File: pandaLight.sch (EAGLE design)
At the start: 162 parts, among them J1 PJ-037A, X1 USBUB-S, X2 HDMI_RECEPTICAL_A, X3 HDMI_RECEPTICAL_A, X4 HDMI_RECEPTICAL_A, Y1 403, Y2 20Mhz

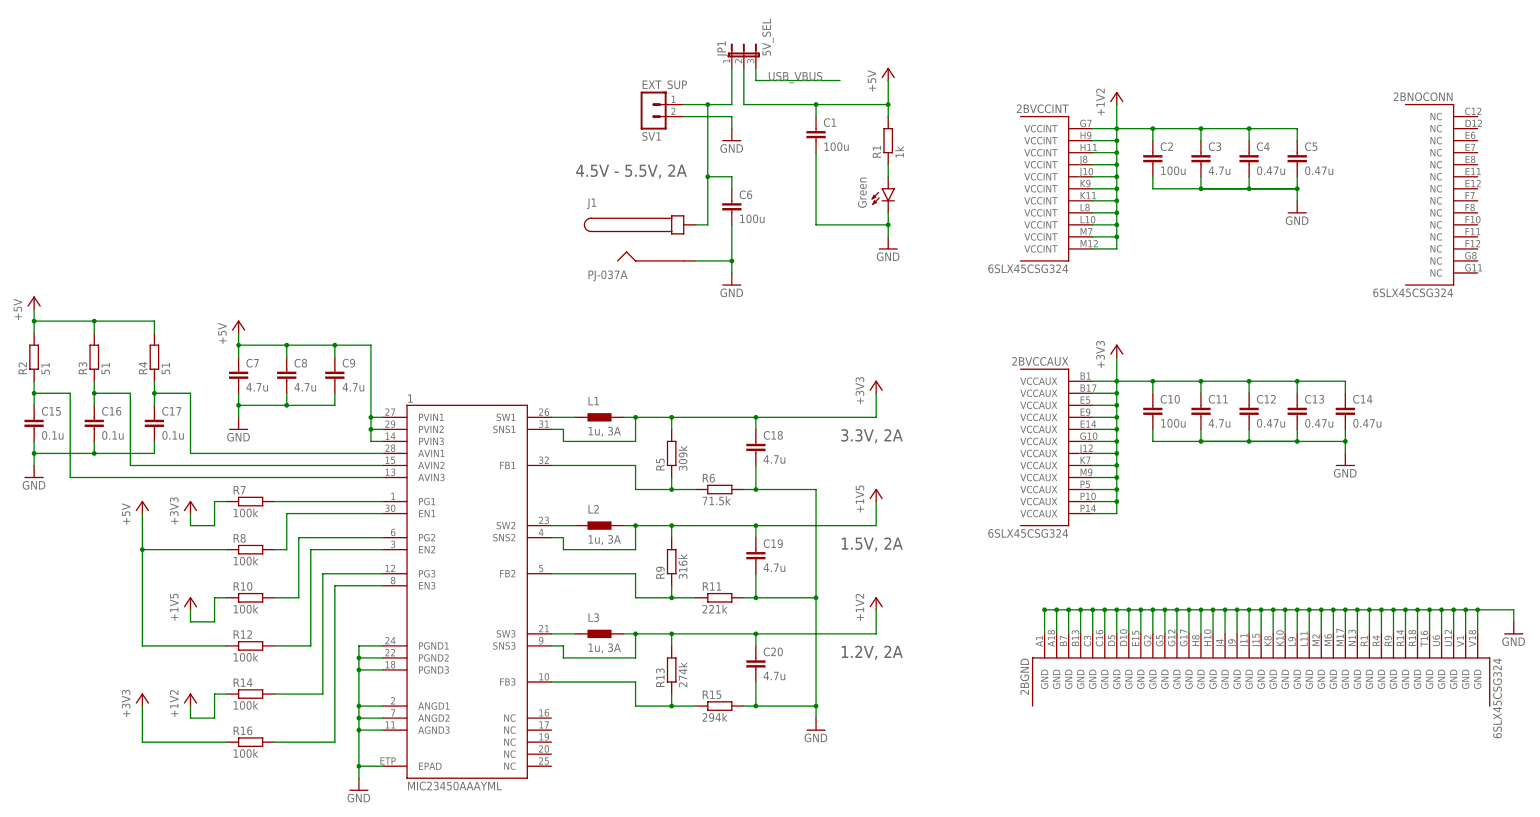
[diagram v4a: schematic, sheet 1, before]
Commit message: Routed the new buck regulator
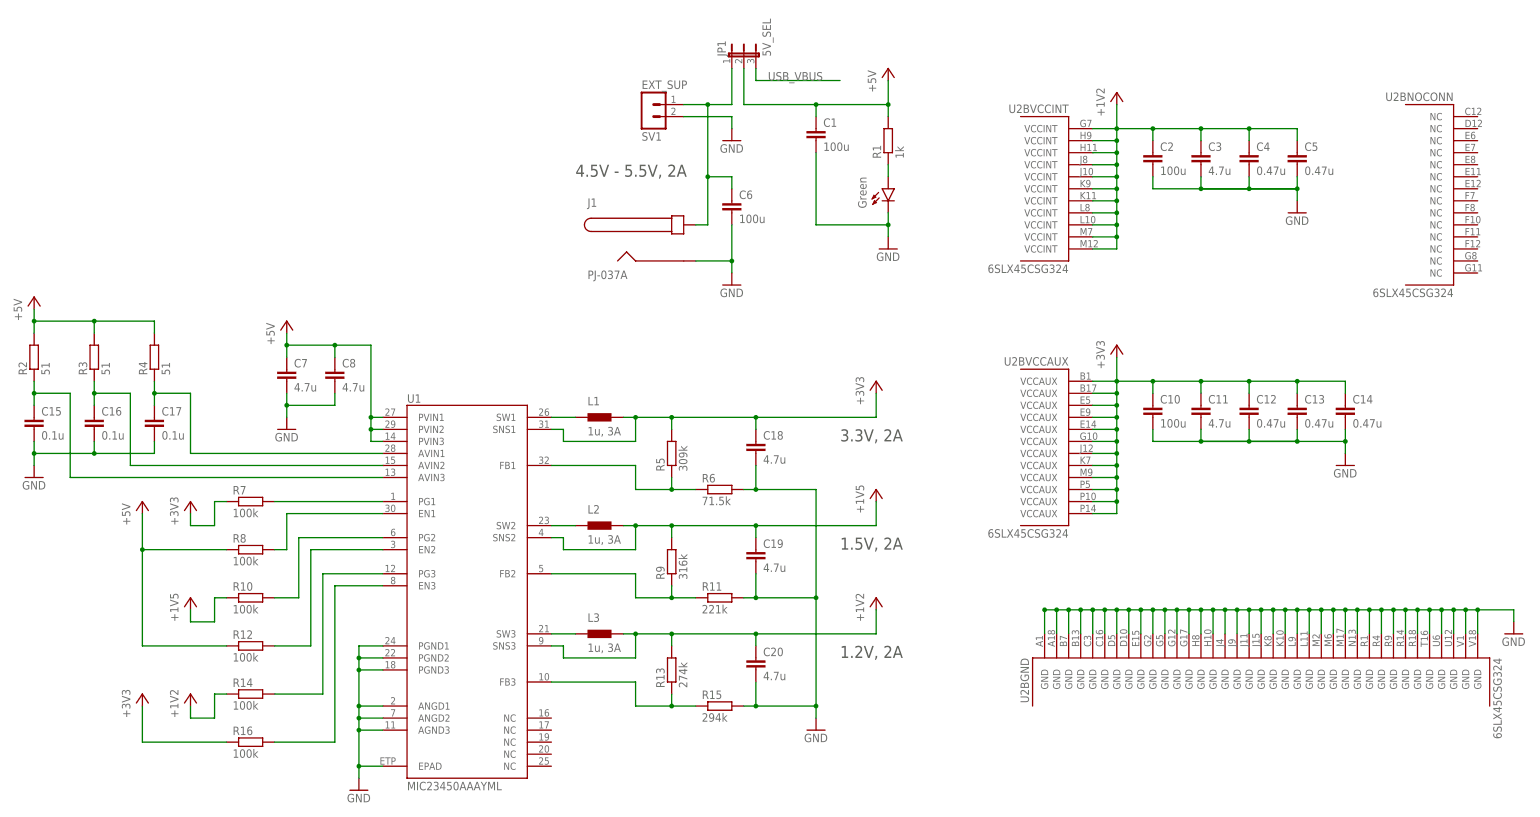
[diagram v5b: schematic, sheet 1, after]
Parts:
- removed C9: 4.7u, pandaLight:CAPACITOR0603
- renumbered 1 to U1, 10 to U10, 11 to U11, 12 to U12, 13 to U13, 14 to U14, 15 to U15, 16 to U16, 17 to U17, 18 to U18, 2 to U2, 3 to U3, 4 to U4, 5 to U5, 6 to U6, 7 to U7, 8 to U8, 9 to U9
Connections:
- net +5V: no longer C9.1
- net GND: no longer C9.2
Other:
- moved on the sheet: C7, C8

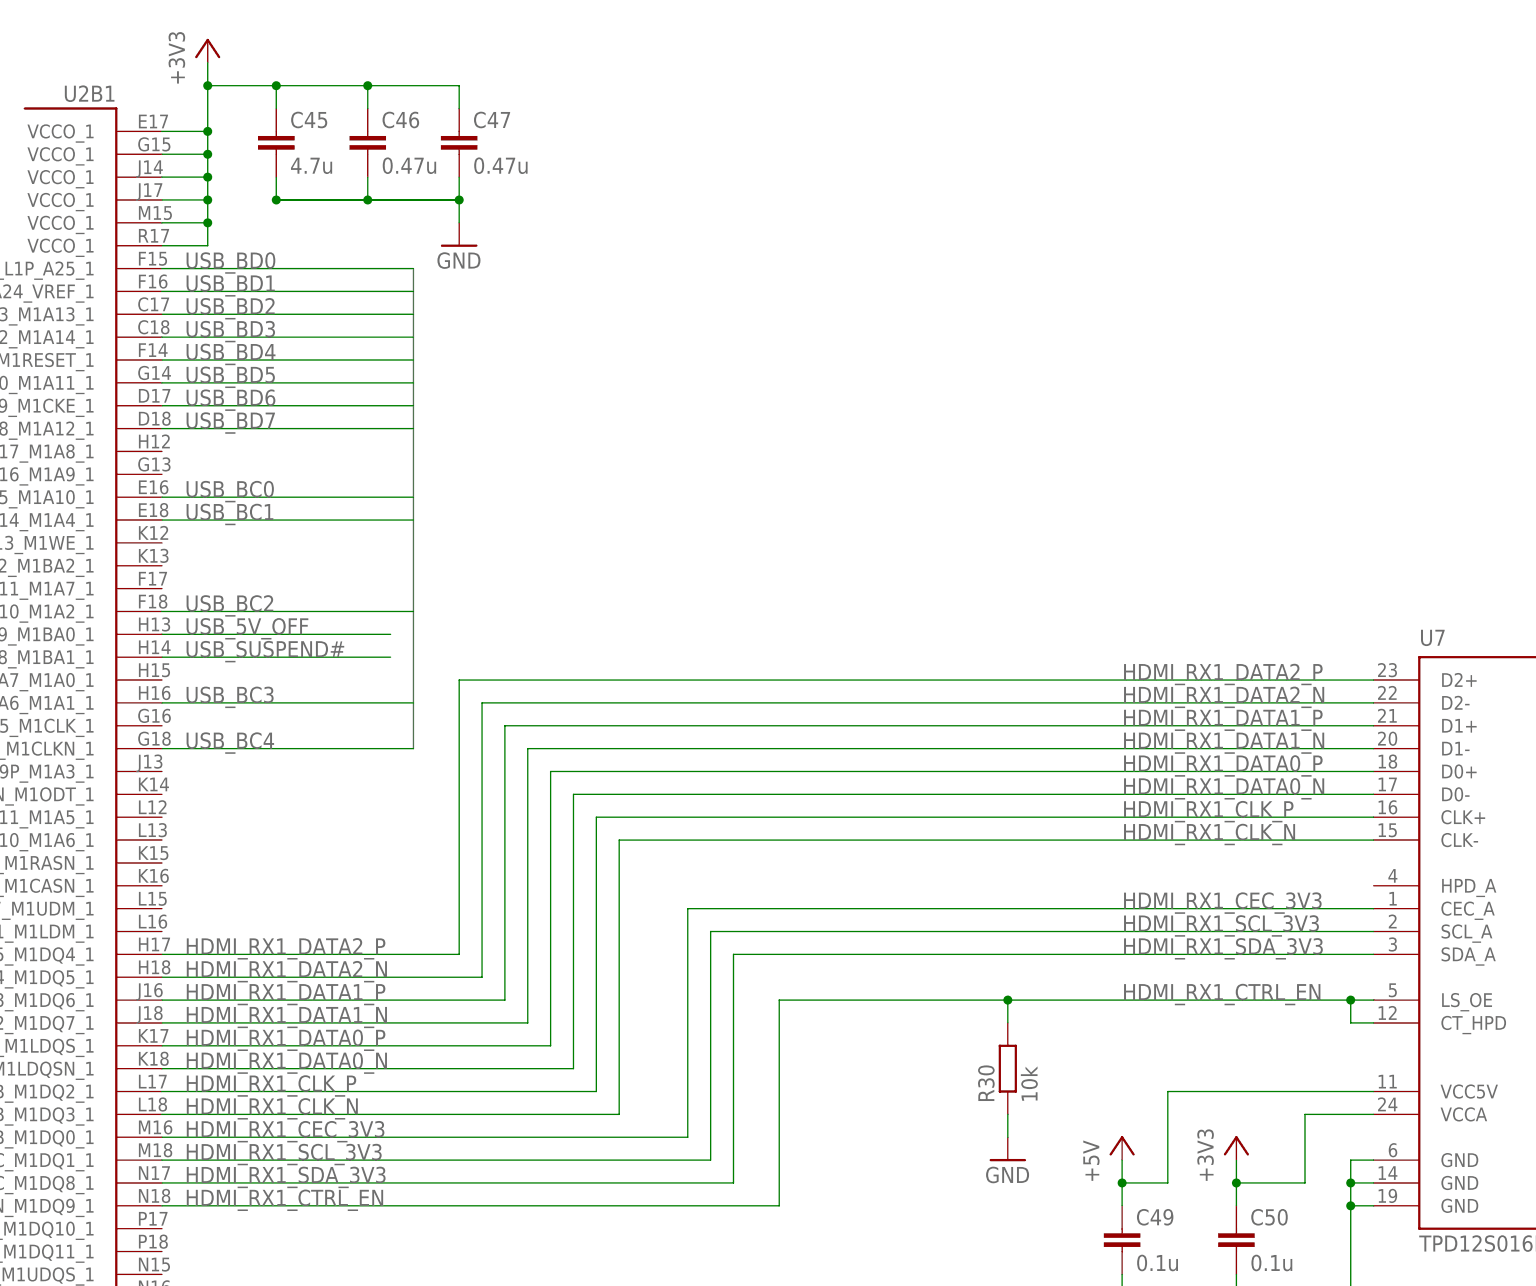
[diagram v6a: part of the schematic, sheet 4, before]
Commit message: Temporarily unconnected the PMOD and USB to FPGA wires; Moved power management and USB a little closer together; Began routing HDMI_RX1
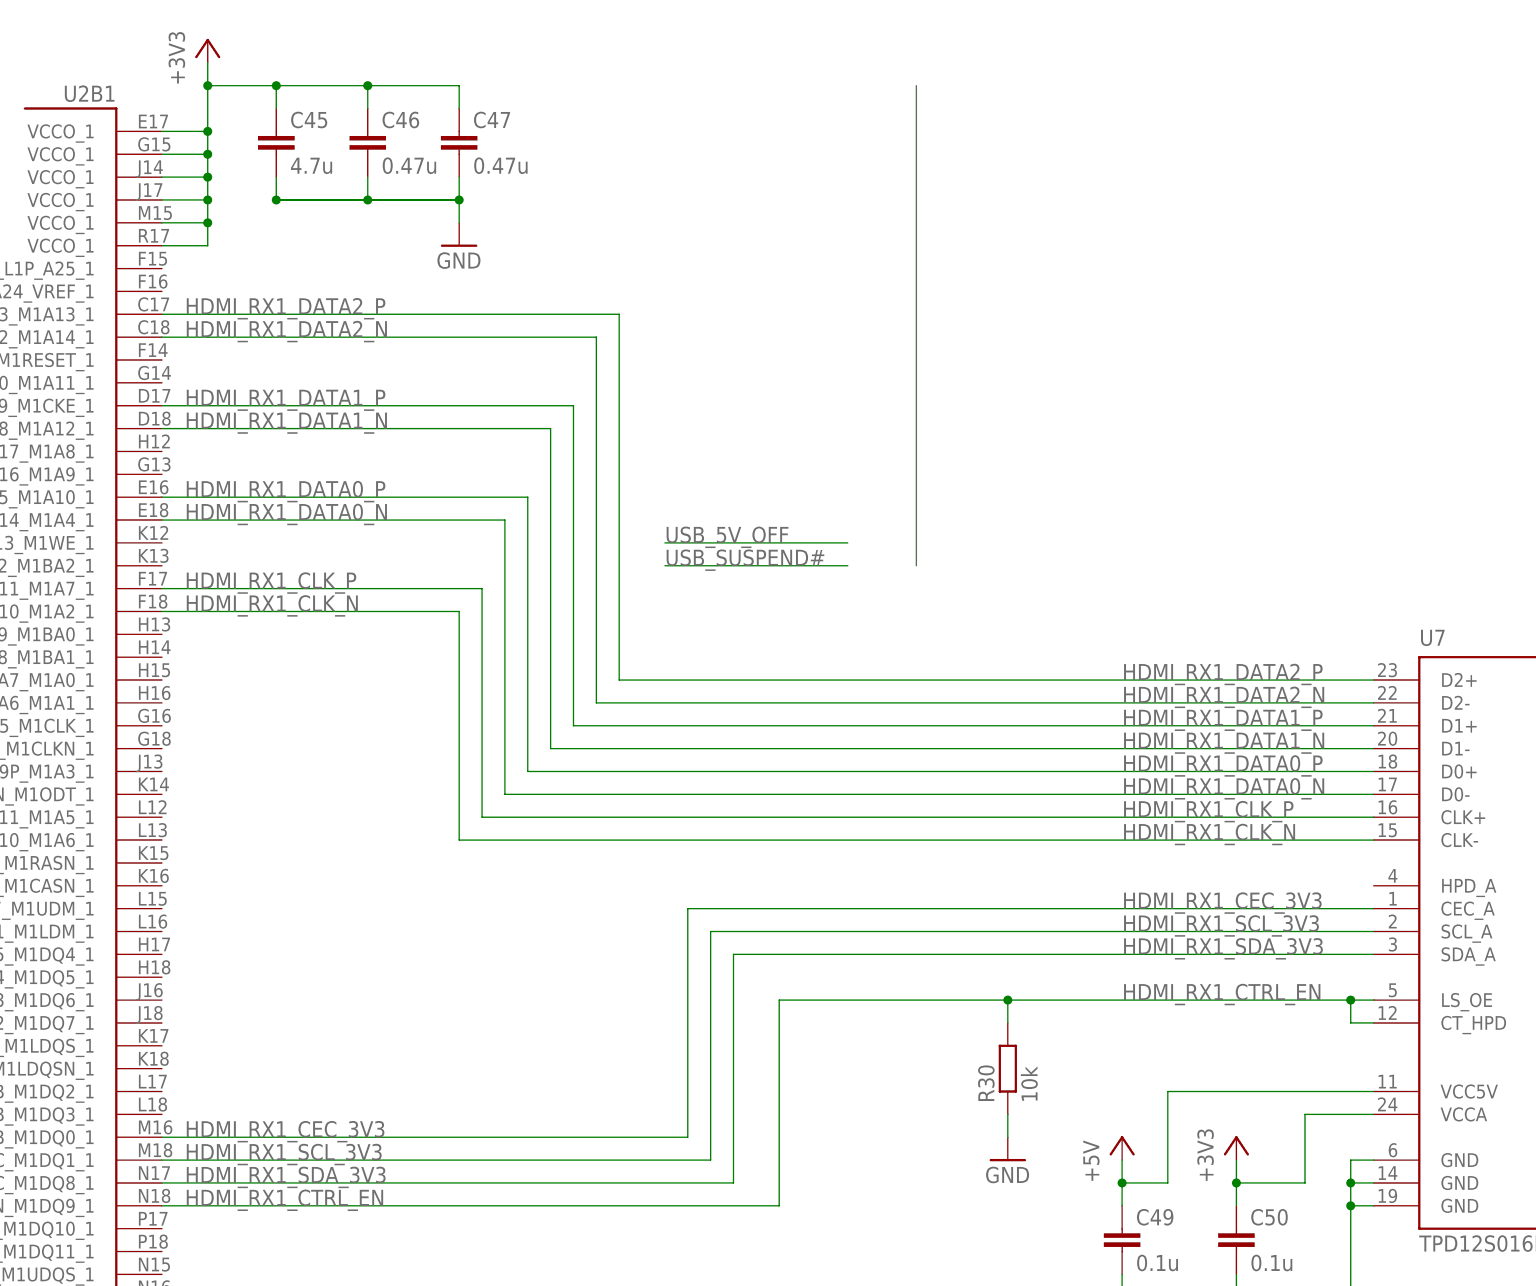
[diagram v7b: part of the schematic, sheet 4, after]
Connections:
- net HDMI_RX1_CLK_N: now also U2B1.IO_L35N_A10_M1A2_1; no longer U2B1.IO_L46N_FOE_B_M1DQ3_1
- net HDMI_RX1_CLK_P: now also U2B1.IO_L35P_A11_M1A7_1; no longer U2B1.IO_L46P_FCS_B_M1DQ2_1
- net HDMI_RX1_DATA0_N: now also U2B1.IO_L33N_A14_M1A4_1; no longer U2B1.IO_L45N_A0_M1LDQSN_1
- net HDMI_RX1_DATA0_P: now also U2B1.IO_L33P_A15_M1A10_1; no longer U2B1.IO_L45P_A1_M1LDQS_1
- net HDMI_RX1_DATA1_N: now also U2B1.IO_L31N_A18_M1A12_1; no longer U2B1.IO_L44N_A2_M1DQ7_1
- net HDMI_RX1_DATA1_P: now also U2B1.IO_L31P_A19_M1CKE_1; no longer U2B1.IO_L44P_A3_M1DQ6_1
- net HDMI_RX1_DATA2_N: now also U2B1.IO_L29N_A22_M1A14_1; no longer U2B1.IO_L43N_GCLK4_M1DQ5_1
- net HDMI_RX1_DATA2_P: now also U2B1.IO_L29P_A23_M1A13_1; no longer U2B1.IO_L43P_GCLK5_M1DQ4_1
- net PMOD0_0: no longer U2B0.IO_L39P_0
- net PMOD0_1: no longer U2B0.IO_L39N_0
- net PMOD0_2: no longer U2B0.IO_L41P_0
- net PMOD0_3: no longer U2B0.IO_L41N_0
- net PMOD1_0: no longer U2B0.IO_L50P_0
- net PMOD1_1: no longer U2B0.IO_L50N_0
- net PMOD1_2: no longer U2B0.IO_L62P_0
- net PMOD1_3: no longer U2B0.IO_L62N_VREF_0
- net PMOD2_0: no longer U2B0.IO_L63P_SCP7_0
- net PMOD2_1: no longer U2B0.IO_L63N_SCP6_0
- net PMOD2_2: no longer U2B0.IO_L64P_SCP5_0
- net PMOD2_3: no longer U2B0.IO_L64N_SCP4_0
- net PMOD3_0: no longer U2B0.IO_L65P_SCP3_0
- net PMOD3_1: no longer U2B0.IO_L65N_SCP2_0
- net PMOD3_2: no longer U2B0.IO_L66P_SCP1_0
- net PMOD3_3: no longer U2B0.IO_L66N_SCP0_0
- net USB_5V_OFF: no longer U2B1.IO_L36P_A9_M1BA0_1
- net USB_BC0: no longer U2B1.IO_L33P_A15_M1A10_1
- net USB_BC1: no longer U2B1.IO_L33N_A14_M1A4_1
- net USB_BC2: no longer U2B1.IO_L35N_A10_M1A2_1
- net USB_BC3: no longer U2B1.IO_L37N_A6_M1A1_1
- net USB_BC4: no longer U2B1.IO_L38N_A4_M1CLKN_1
- net USB_BD0: no longer U2B1.IO_L1P_A25_1
- net USB_BD1: no longer U2B1.IO_L1N_A24_VREF_1
- net USB_BD2: no longer U2B1.IO_L29P_A23_M1A13_1
- net USB_BD3: no longer U2B1.IO_L29N_A22_M1A14_1
- net USB_BD4: no longer U2B1.IO_L30P_A21_M1RESET_1
- net USB_BD5: no longer U2B1.IO_L30N_A20_M1A11_1
- net USB_BD6: no longer U2B1.IO_L31P_A19_M1CKE_1
- net USB_BD7: no longer U2B1.IO_L31N_A18_M1A12_1
- net USB_SUSPEND#: no longer U2B1.IO_L36N_A8_M1BA1_1
